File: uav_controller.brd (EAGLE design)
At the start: 100 x 80 mm, 20 parts, among them IC1 PIC16F877SO, U1 L298, U2 L298, U3 LCD-16X28X2

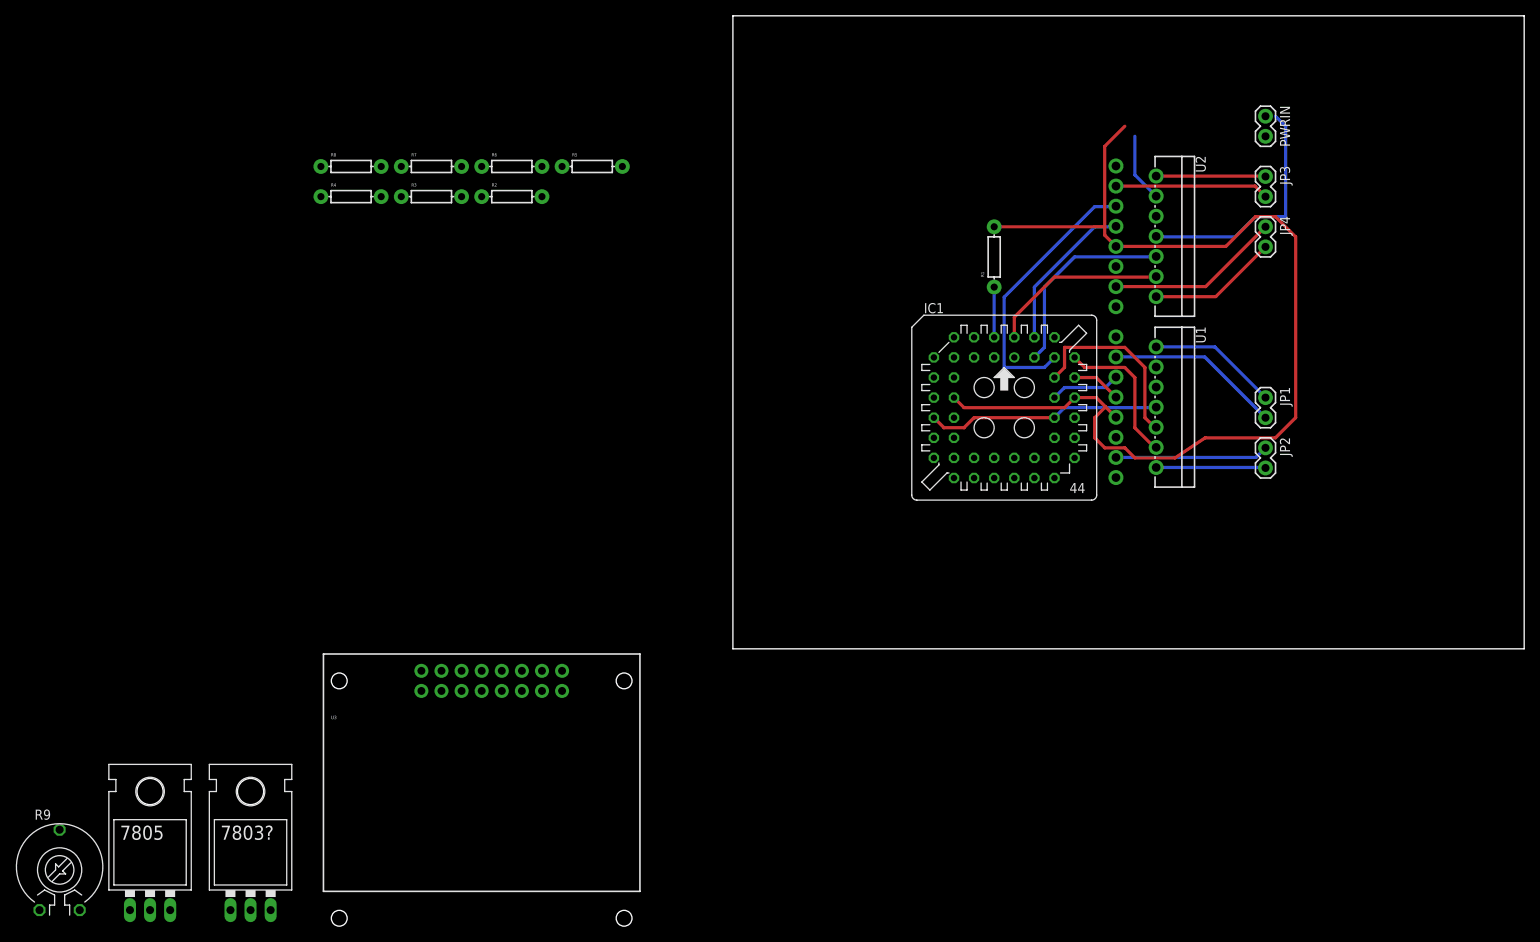
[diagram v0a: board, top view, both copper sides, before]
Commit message: Added L3G4200D 3-Axis Gyro Carrier, not using the internal vreg. http://www.pololu.com/catalog/product/1272
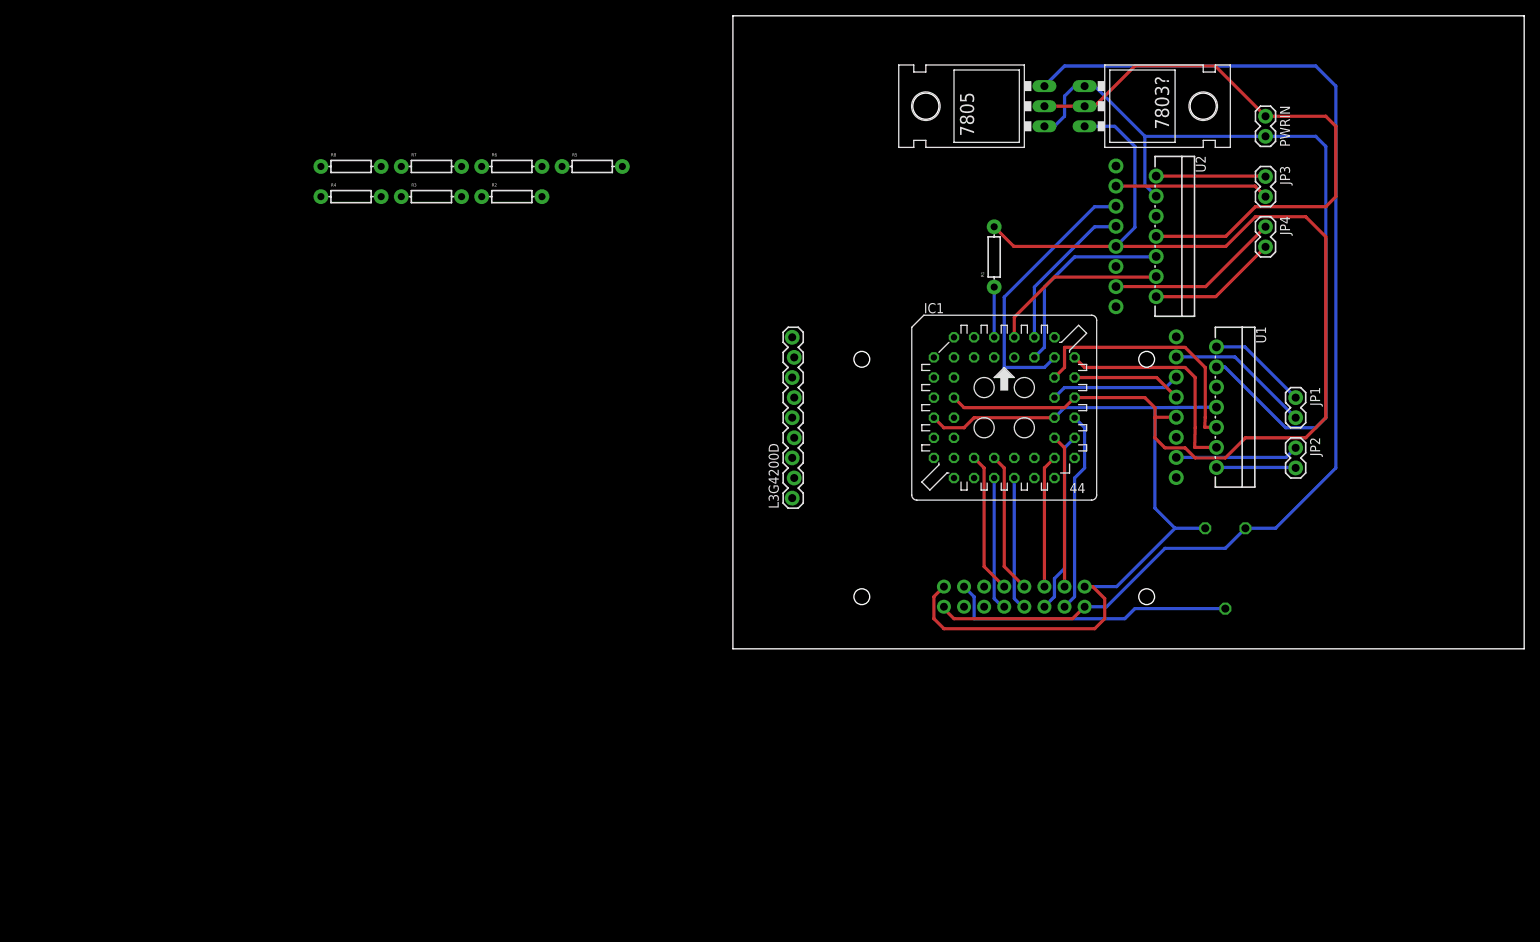
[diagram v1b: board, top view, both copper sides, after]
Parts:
- added L3G4200D: M09LOCK, SparkFun-Connectors:1X09_LOCK
- moved R9 152.2 mm to (62.2, 10.2), flipped to the bottom, turned to 180 degrees
- moved 7803? 146.6 mm to (48.3, 68.6), turned to 270 degrees
- moved 7805 146.6 mm to (35.6, 68.6), turned to 90 degrees
- moved U3 77.5 mm to (34.3, 21.6), flipped to the bottom, turned to 180 degrees
- moved U1 7.62 mm to (58.4, 30.5)
- moved JP1 3.81 mm to (71.1, 31.8)
- moved JP2 3.81 mm to (71.1, 25.4)
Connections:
- removed net N$19: IC1.23
- removed net N$20: IC1.24
- removed net N$21: IC1.25
- new net I2C_SCL: IC1.20, L3G4200D.6
- new net I2C_SDA: IC1.25, L3G4200D.5
- new net N$10: IC1.26
- new net N$11: IC1.27
- new net N$12: IC1.29
- net 3.3V: now also L3G4200D.7
- net D_D0: now also IC1.21
- net D_D1: now also IC1.22
- net D_D2: now also IC1.23
- net D_D3: now also IC1.24
- net D_D4: now also IC1.30
- net D_D5: now also IC1.31
- net D_D6: now also IC1.32
- net D_D7: now also IC1.33
- net GND: now also L3G4200D.8
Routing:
- net 5V: track 0.00 -> 145.4 mm
- net GND: track 60.4 -> 180.6 mm
- net VCC: track 8.67 -> 102.3 mm
- net D_DIM: track 0.00 -> 36.9 mm
- net D_D7: track 0.00 -> 25.5 mm
- net D_D5: track 0.00 -> 22.9 mm
- net D_D6: track 0.00 -> 19.3 mm
- net D_D0: track 0.00 -> 17.8 mm
- net D_D2: track 0.00 -> 17.8 mm
- net D_D1: track 0.00 -> 16.9 mm
- net D_D3: track 0.00 -> 16.9 mm
- net D_D4: track 0.00 -> 16.8 mm
- net 3.3V: track 134.3 -> 147.7 mm
- net FWD4: track 18.7 -> 27.9 mm
- net FWD3: track 23.8 -> 32.2 mm
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
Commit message: Added OSC and connectors for analog range finders: http://www.pololu.com/catalog/product/136
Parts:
- added JP5: (no value), SparkFun-Connectors:1X03
- added RANGE_DOWN, RANGE_FORE, RANGE_UP: (no value), SparkFun-Connectors:JST-3-PTH
- added Y1: (no value), SparkFun-FreqCtrl:RESONATOR-PTH
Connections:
- new net DIST_DOWN: IC1.10, RANGE_DOWN.1
- new net DIST_FORE: IC1.9, RANGE_FORE.1
- new net DIST_UP: IC1.11, RANGE_UP.1
- new net N$17: JP5.2, RANGE_DOWN.3, RANGE_FORE.3, RANGE_UP.3
- new net OSC1: IC1.14, Y1.1
- new net OSC2: IC1.15, Y1.3
- net 3.3V: now also JP5.1
- net 5V: now also JP5.3
- net GND: now also RANGE_DOWN.2, RANGE_FORE.2, RANGE_UP.2, Y1.2
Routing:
- net GND: track 180.6 -> 241.3 mm
- net N$17: track 0.00 -> 42.4 mm
- net DIST_DOWN: track 0.00 -> 39.4 mm
- net 3.3V: track 147.7 -> 183.5 mm
- net I2C_SDA: track 0.00 -> 30.2 mm
- net DIST_FORE: track 0.00 -> 29.5 mm
- net I2C_SCL: track 0.00 -> 28.4 mm
- net DIST_UP: track 0.00 -> 23.9 mm
- net 5V: track 145.4 -> 161.7 mm
- net OSC1: track 0.00 -> 15.9 mm
- net OSC2: track 0.00 -> 7.18 mm
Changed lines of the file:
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@@
 <element name="R9" library="pot" package="PT-10" value="" x="62.23" y="10.16" rot="MR180"/>
 <element name="L3G4200D" library="SparkFun-Connectors" package="1X09_LOCK" value="M09LOCK" x="7.62" y="19.05" rot="R90"/>
+<element name="RANGE_UP" library="SparkFun-Connectors" package="JST-3-PTH" value="" x="2.54" y="48.26" rot="R90"/>
+<element name="RANGE_DOWN" library="SparkFun-Connectors" package="JST-3-PTH" value="" x="2.54" y="66.04" rot="R90"/>
+<element name="RANGE_FORE" library="SparkFun-Connectors" package="JST-3-PTH" value="" x="2.54" y="57.15" rot="R90"/>
+<element name="JP5" library="SparkFun-Connectors" package="1X03" value="" x="26.67" y="60.96"/>
+<element name="Y1" library="SparkFun-FreqCtrl" package="RESONATOR-PTH" value="" x="17.78" y="21.59"/>
 </elements>
 <signals>
@@
 <wire x1="74.93" y1="67.31" x2="67.31" y2="67.31" width="0.4064" layer="1"/>
 <contactref element="L3G4200D" pad="8"/>
+<wire x1="7.747" y1="36.83" x2="11.43" y2="36.83" width="0.4064" layer="16"/>
+<wire x1="11.43" y1="36.83" x2="16.51" y2="31.75" width="0.4064" layer="16"/>
+<wire x1="16.51" y1="31.75" x2="22.86" y2="31.75" width="0.4064" layer="16"/>
+<wire x1="22.86" y1="31.75" x2="25.4" y2="29.21" width="0.4064" layer="16"/>
+<contactref element="RANGE_UP" pad="2"/>
+<contactref element="RANGE_DOWN" pad="2"/>
+<contactref element="RANGE_FORE" pad="2"/>
+<wire x1="7.54" y1="48.26" x2="6.35" y2="49.53" width="0.4064" layer="16"/>
+<wire x1="6.35" y1="49.53" x2="6.35" y2="55.88" width="0.4064" layer="16"/>
+<wire x1="6.35" y1="55.88" x2="7.54" y2="57.15" width="0.4064" layer="16"/>
+<wire x1="7.54" y1="48.26" x2="6.35" y2="47.07" width="0.4064" layer="16"/>
+<wire x1="6.35" y1="47.07" x2="6.35" y2="38.1" width="0.4064" layer="16"/>
+<wire x1="6.35" y1="38.1" x2="7.62" y2="36.83" width="0.4064" layer="16"/>
+<wire x1="7.62" y1="36.83" x2="7.747" y2="36.83" width="0.4064" layer="16"/>
+<contactref element="Y1" pad="2"/>
+<wire x1="17.78" y1="21.59" x2="25.4" y2="13.97" width="0.4064" layer="1"/>
+<wire x1="25.4" y1="13.97" x2="25.4" y2="8.89" width="0.4064" layer="1"/>
+<wire x1="25.4" y1="8.89" x2="26.43" y2="7.86" width="0.4064" layer="1"/>
+<wire x1="26.43" y1="7.86" x2="26.67" y2="7.86" width="0.4064" layer="1"/>
 <wire x1="61.11" y1="30.54" x2="62.29" y2="52.13" width="0" layer="19" extent="1-1"/>
-<wire x1="7.747" y1="36.83" x2="25.4" y2="29.21" width="0" layer="19" extent="1-1"/>
+<wire x1="7.54" y1="66.04" x2="7.54" y2="57.15" width="0" layer="19" extent="1-1"/>
 </signal>
 <signal name="3.3V">
@@
 <wire x1="35.5" y1="50.86" x2="33.02" y2="53.34" width="0.4064" layer="1"/>
 <contactref element="L3G4200D" pad="7"/>
-<wire x1="7.493" y1="34.29" x2="27.94" y2="31.75" width="0" layer="19" extent="1-1"/>
+<wire x1="7.493" y1="34.29" x2="22.86" y2="34.29" width="0.4064" layer="1"/>
+<wire x1="22.86" y1="34.29" x2="24.13" y2="33.02" width="0.4064" layer="1"/>
+<wire x1="24.13" y1="33.02" x2="26.67" y2="33.02" width="0.4064" layer="1"/>
+<wire x1="26.67" y1="33.02" x2="27.94" y2="31.75" width="0.4064" layer="1"/>
+<contactref element="JP5" pad="1"/>
+<wire x1="33.02" y1="53.34" x2="30.48" y2="55.88" width="0.4064" layer="1"/>
+<wire x1="30.48" y1="55.88" x2="30.48" y2="62.23" width="0.4064" layer="1"/>
+<wire x1="30.48" y1="62.23" x2="27.94" y2="62.23" width="0.4064" layer="1"/>
+<wire x1="27.94" y1="62.23" x2="26.67" y2="60.96" width="0.4064" layer="1"/>
 </signal>
 <signal name="VCC">
@@
 <wire x1="73.66" y1="73.66" x2="41.91" y2="73.66" width="0.4064" layer="16"/>
 <wire x1="41.91" y1="73.66" x2="39.37" y2="71.12" width="0.4064" layer="16"/>
+<contactref element="JP5" pad="3"/>
+<wire x1="31.75" y1="60.96" x2="31.75" y2="68.58" width="0.4064" layer="1"/>
+<wire x1="31.75" y1="68.58" x2="34.29" y2="71.12" width="0.4064" layer="1"/>
+<wire x1="34.29" y1="71.12" x2="39.37" y2="71.12" width="0.4064" layer="1"/>
 </signal>
 <signal name="D_DIM">
@@
 <contactref element="L3G4200D" pad="6"/>
 <contactref element="IC1" pad="20"/>
-<wire x1="7.747" y1="31.75" x2="30.48" y2="21.59" width="0" layer="19" extent="1-1"/>
+<wire x1="7.747" y1="31.75" x2="16.51" y2="31.75" width="0.4064" layer="1"/>
+<wire x1="16.51" y1="31.75" x2="22.86" y2="25.4" width="0.4064" layer="1"/>
+<wire x1="22.86" y1="25.4" x2="29.21" y2="25.4" width="0.4064" layer="1"/>
+<wire x1="29.21" y1="25.4" x2="29.21" y2="22.86" width="0.4064" layer="1"/>
+<wire x1="29.21" y1="22.86" x2="30.48" y2="21.59" width="0.4064" layer="1"/>
 </signal>
 <signal name="I2C_SDA">
 <contactref element="L3G4200D" pad="5"/>
 <contactref element="IC1" pad="25"/>
-<wire x1="7.493" y1="29.21" x2="35.56" y2="24.13" width="0" layer="19" extent="1-1"/>
+<wire x1="7.493" y1="29.21" x2="19.05" y2="29.21" width="0.4064" layer="16"/>
+<wire x1="19.05" y1="29.21" x2="22.86" y2="25.4" width="0.4064" layer="16"/>
+<wire x1="22.86" y1="25.4" x2="34.29" y2="25.4" width="0.4064" layer="16"/>
+<wire x1="34.29" y1="25.4" x2="35.56" y2="24.13" width="0.4064" layer="16"/>
+</signal>
+<signal name="DIST_UP">
+<contactref element="RANGE_UP" pad="1"/>
+<contactref element="IC1" pad="11"/>
+<wire x1="7.54" y1="46.26" x2="10.89" y2="46.26" width="0.4064" layer="16"/>
+<wire x1="10.89" y1="46.26" x2="25.4" y2="31.75" width="0.4064" layer="16"/>
+</signal>
+<signal name="DIST_DOWN">
+<contactref element="RANGE_DOWN" pad="1"/>
+<contactref element="IC1" pad="10"/>
+<wire x1="27.94" y1="34.29" x2="26.67" y2="35.56" width="0.4064" layer="16"/>
+<wire x1="26.67" y1="35.56" x2="26.67" y2="38.1" width="0.4064" layer="16"/>
+<wire x1="26.67" y1="38.1" x2="12.7" y2="52.07" width="0.4064" layer="16"/>
+<wire x1="12.7" y1="52.07" x2="12.7" y2="60.96" width="0.4064" layer="16"/>
+<wire x1="12.7" y1="60.96" x2="9.62" y2="64.04" width="0.4064" layer="16"/>
+<wire x1="9.62" y1="64.04" x2="7.54" y2="64.04" width="0.4064" layer="16"/>
+</signal>
+<signal name="DIST_FORE">
+<contactref element="RANGE_FORE" pad="1"/>
+<contactref element="IC1" pad="9"/>
+<wire x1="25.4" y1="34.29" x2="11.43" y2="48.26" width="0.4064" layer="16"/>
+<wire x1="11.43" y1="48.26" x2="11.43" y2="53.34" width="0.4064" layer="16"/>
+<wire x1="11.43" y1="53.34" x2="9.62" y2="55.15" width="0.4064" layer="16"/>
+<wire x1="9.62" y1="55.15" x2="7.54" y2="55.15" width="0.4064" layer="16"/>
+</signal>
+<signal name="N$17">
+<contactref element="JP5" pad="2"/>
+<contactref element="RANGE_FORE" pad="3"/>
+<contactref element="RANGE_DOWN" pad="3"/>
+<contactref element="RANGE_UP" pad="3"/>
+<wire x1="7.54" y1="50.26" x2="6.35" y2="51.45" width="0.4064" layer="1"/>
+<wire x1="6.35" y1="51.45" x2="6.35" y2="58.42" width="0.4064" layer="1"/>
+<wire x1="6.35" y1="58.42" x2="7.08" y2="59.15" width="0.4064" layer="1"/>
+<wire x1="7.08" y1="59.15" x2="7.54" y2="59.15" width="0.4064" layer="1"/>
+<wire x1="7.54" y1="68.04" x2="6.35" y2="66.85" width="0.4064" layer="1"/>
+<wire x1="6.35" y1="66.85" x2="6.35" y2="60.34" width="0.4064" layer="1"/>
+<wire x1="7.54" y1="59.15" x2="6.35" y2="60.34" width="0.4064" layer="1"/>
+<wire x1="29.21" y1="60.96" x2="27.4" y2="59.15" width="0.4064" layer="1"/>
+<wire x1="27.4" y1="59.15" x2="7.54" y2="59.15" width="0.4064" layer="1"/>
+</signal>
+<signal name="OSC2">
+<contactref element="Y1" pad="3"/>
+<contactref element="IC1" pad="15"/>
+<wire x1="20.32" y1="21.59" x2="25.4" y2="26.67" width="0.4064" layer="16"/>
+</signal>
+<signal name="OSC1">
+<contactref element="Y1" pad="1"/>
+<contactref element="IC1" pad="14"/>
+<wire x1="27.94" y1="29.21" x2="26.67" y2="27.94" width="0.4064" layer="16"/>
+<wire x1="26.67" y1="27.94" x2="21.59" y2="27.94" width="0.4064" layer="16"/>
+<wire x1="21.59" y1="27.94" x2="15.24" y2="21.59" width="0.4064" layer="16"/>
 </signal>
 </signals>
